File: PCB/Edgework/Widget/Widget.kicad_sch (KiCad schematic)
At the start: 41 parts, among them J1 Edgework, J10 4, J11 SDA, J12 SCL, J13 1, J14 0, J15 5V, J16 3V3, J17 GND, J18 5V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

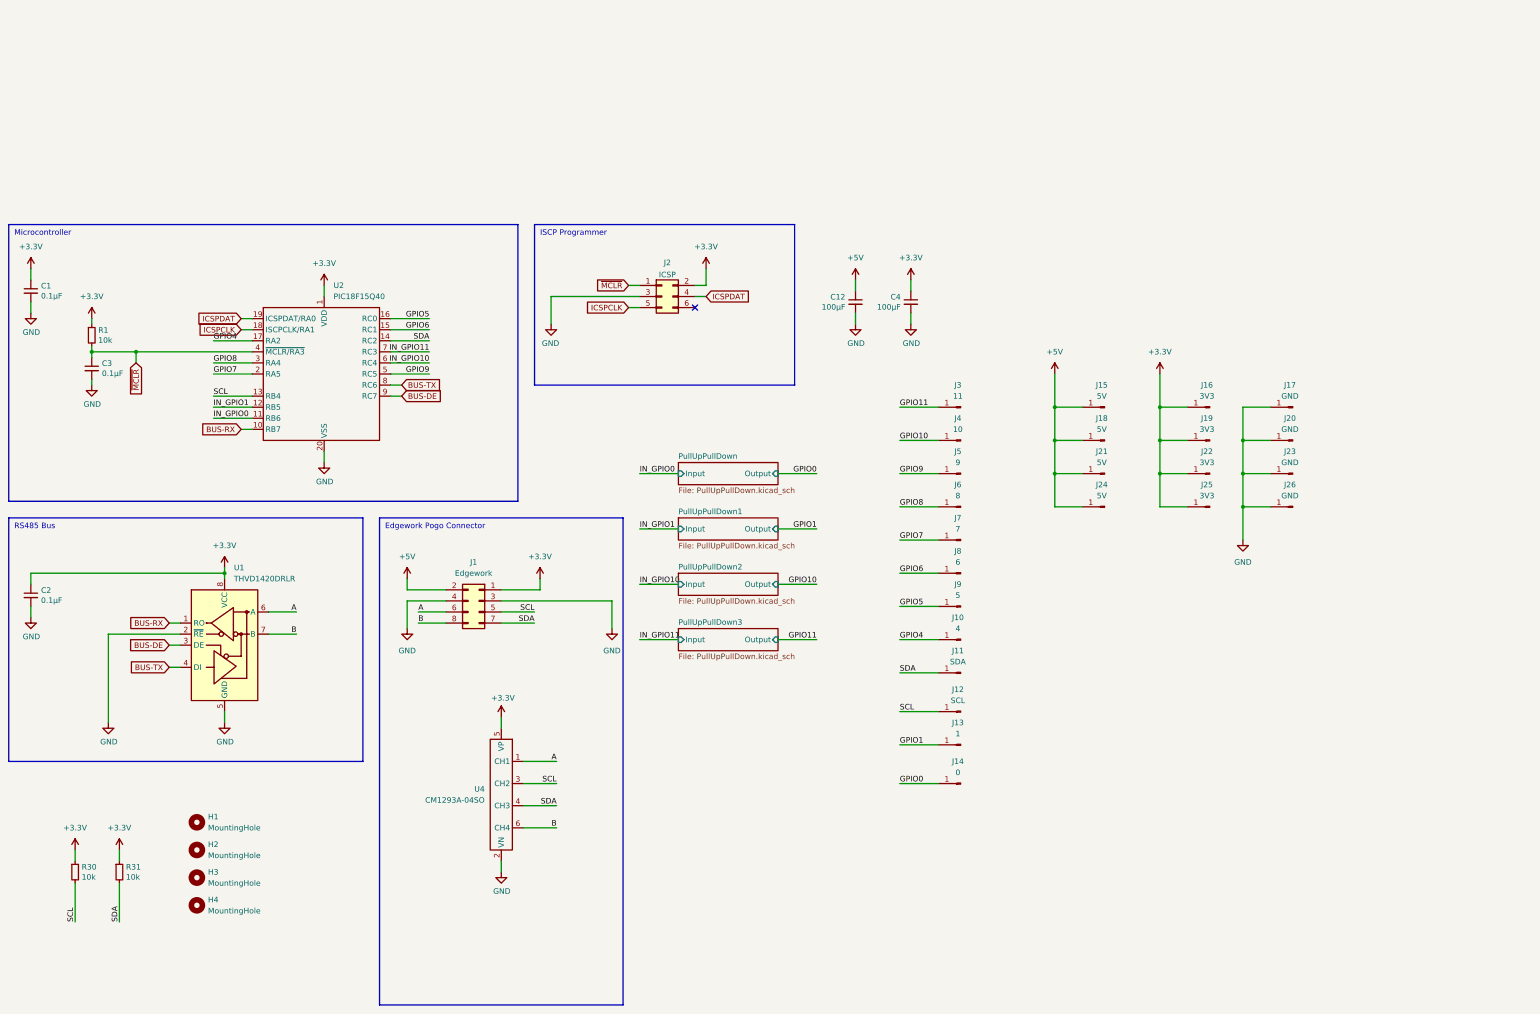
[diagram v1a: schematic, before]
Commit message: feat: Migrate edgework to a STM32G070KBT6.
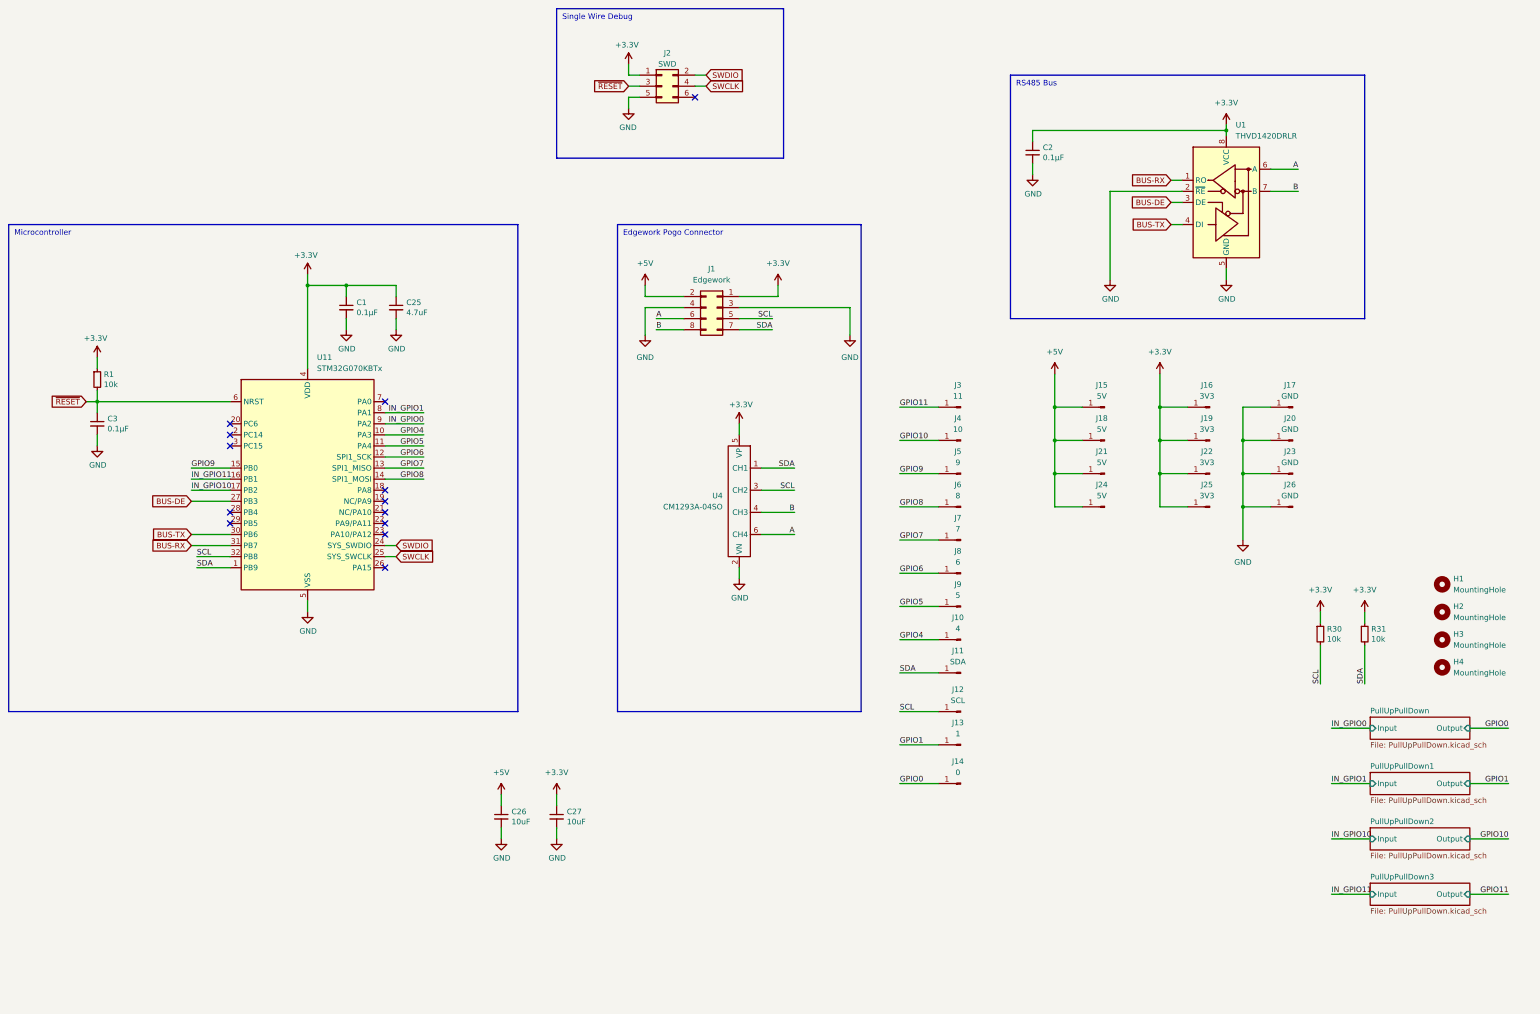
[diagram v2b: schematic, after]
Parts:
- removed C12, C4: 100μF, Capacitor_SMD:C_1206_3216Metric, symbol Device:C_Small
- removed U2: PIC18F15Q40, Package_SO:SSOP-20_5.3x7.2mm_P0.65mm, symbol KTANE:PIC18F15Q40
- added C25: 4.7uF, Capacitor_SMD:C_0603_1608Metric, symbol Device:C_Small
- added C26, C27: 10uF, Capacitor_SMD:C_0603_1608Metric, symbol Device:C_Small
- added U11: STM32G070KBTx, Package_QFP:LQFP-32_7x7mm_P0.8mm, symbol KTANE:STM32G070KBTx
- H1, H2, H3, H4: footprint MountingHole:MountingHole_3.2mm_M3 -> KTANE:MountingHole_3.2mm_M3_NoCopper
- J2: value ICSP -> SWD
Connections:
- net ICSPCLK is gone; now on net GND: J2.5 (Pin_5)
- net +3.3V: now also J2.1 (Pin_1), C25.1, C27.1, U11.4 (VDD); no longer J2.2 (Pin_2)
- net +5V: now also C26.1
- net A: now also U4.6 (CH4); no longer U4.1 (CH1)
- net B: now also U4.4 (CH3); no longer U4.6 (CH4)
- net BUS-DE: now also U11.27 (PB3)
- net BUS-RX: now also U11.31 (PB7)
- net BUS-TX: now also U11.30 (PB6)
- net GND: now also C25.2, C26.2, C27.2, U11.5 (VSS); no longer J2.3 (Pin_3)
- net GPIO4: now also U11.10 (PA3)
- net GPIO5: now also U11.11 (PA4)
- net GPIO6: now also U11.12 (PA5)
- net GPIO7: now also U11.13 (PA6)
- net GPIO8: now also U11.14 (PA7)
- net GPIO9: now also U11.15 (PB0)
- net IN_GPIO0: now also U11.9 (PA2)
- net IN_GPIO1: now also U11.8 (PA1)
- net IN_GPIO10: now also U11.17 (PB2)
- net IN_GPIO11: now also U11.16 (PB1)
- net SCL: now also U11.32 (PB8)
- net SDA: now also U4.1 (CH1), U11.1 (PB9); no longer U4.4 (CH3)
- net ICSPDAT renamed SWCLK
- net SWCLK: now also U11.25 (PA14)
- net ~{MCLR} renamed ~{RESET}
- net ~{RESET}: now also J2.3 (Pin_3), U11.6 (NRST); no longer J2.1 (Pin_1)
- new net SWDIO: J2.2 (Pin_2), U11.24 (PA13)
- no-connect marks 1 -> 13
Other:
- note added: "Single Wire Debug"
- note removed: "ISCP Programmer"
- moved on the sheet: C1, C2, C3, H1, H2, H3, H4, J1, J2, R1, R30, R31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

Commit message: feat: Export new revision BOM, allow in .gitignore, fix up revisions in schematics.
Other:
- title: (none) -> Edgework Widget
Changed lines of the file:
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@@
 	(generator_version "10.0")
 	(paper "A4")
+	(title_block
+		(title "Edgework Widget")
+		(rev "B01")
+	)
 	(rectangle
 		(start 245.11 -19.05)
